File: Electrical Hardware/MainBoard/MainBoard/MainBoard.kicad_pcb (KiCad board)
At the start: 2 copper layers, 49.4 x 51.7 mm, 76 parts, among them J1 SM02B-SRSS-TB_LFSN_, J2 Conn_01x04_Socket, J3 Conn_01x04_Socket, J4 Conn_01x04_Socket, J5 USB_B_Micro, J6 Thermistor, J7 62684-401100ALF, J8 Conn_01x02_Socket, SW1 SW_Push, SW2 SW_Push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

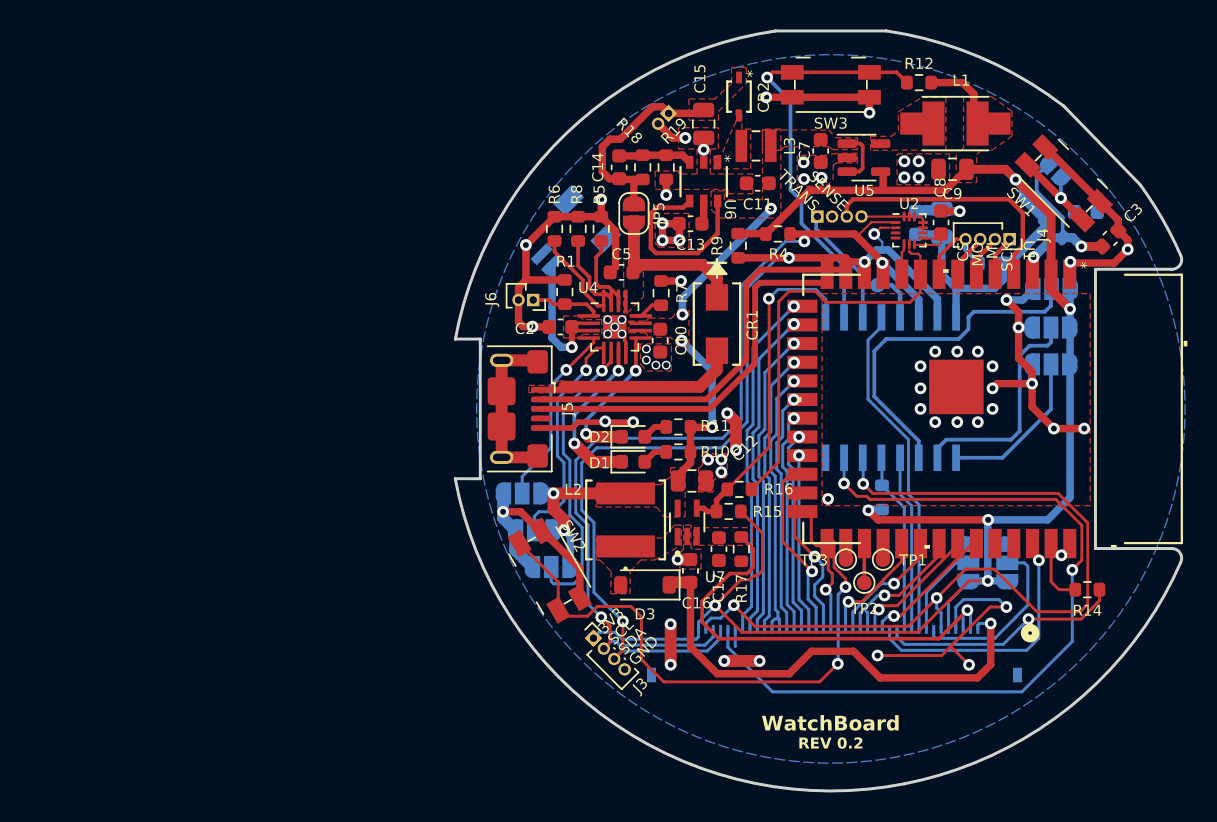
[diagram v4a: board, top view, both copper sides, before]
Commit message: Add potential new USB C port; make minor layout edits
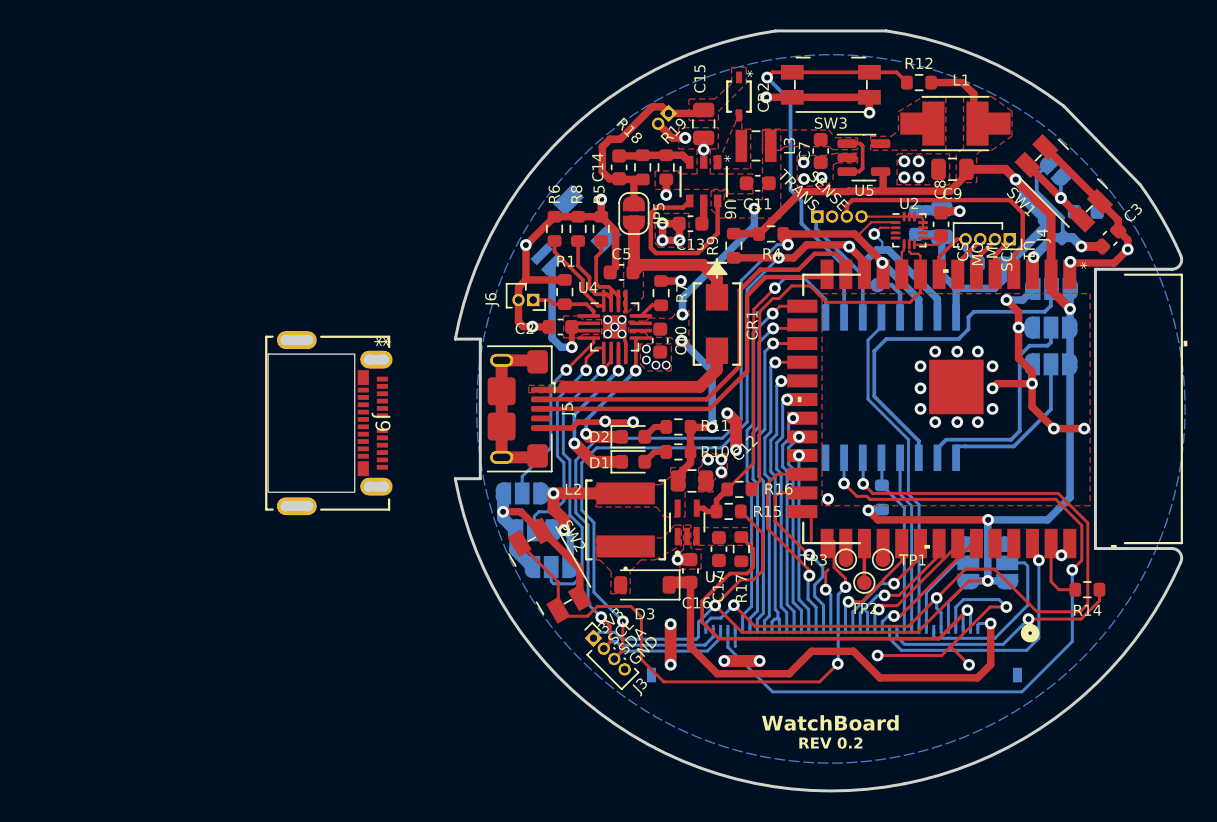
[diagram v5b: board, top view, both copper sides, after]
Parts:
- added J9: 1054550101, 1054550101:105455-0101_MOL, F.Cu at (59.5, 51.9)
- moved R4 0.46 mm to (89.7, 39.0)
- moved R9 0.30 mm to (87.1, 39.8)
- moved C8 0.13 mm to (101.2, 38.4)
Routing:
- net /B5: track 9.09 -> 6.26 mm
- net /G0: track 11.4 -> 13.5 mm
- net D-: track 28.2 -> 29.8 mm
- net /G1: track 13.4 -> 14.6 mm
- net /R3: track 21.9 -> 22.8 mm
- net /SDA: track 68.9 -> 69.7 mm
- net /BACKLIGHT: track 23.0 -> 23.7 mm
- net /R2: track 20.4 -> 21.2 mm
- net A1: track 27.6 -> 28.2 mm
- net /SCL: track 65.8 -> 66.5 mm
- net /R4: track 23.5 -> 24.1 mm
- net /R5: track 24.9 -> 25.4 mm
- net +3.3V: track 144.4 -> 144.9 mm
- net /R1: track 20.1 -> 20.6 mm

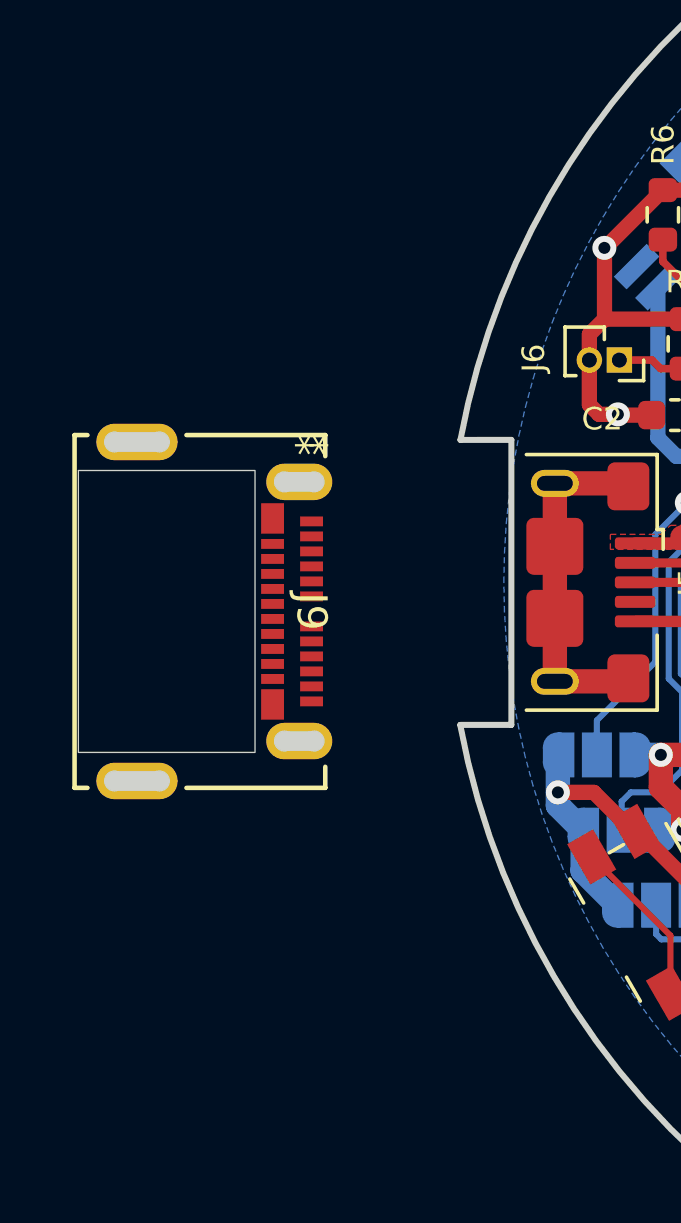
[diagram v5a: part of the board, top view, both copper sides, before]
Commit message: Add another potential USB-C with simplified pinout
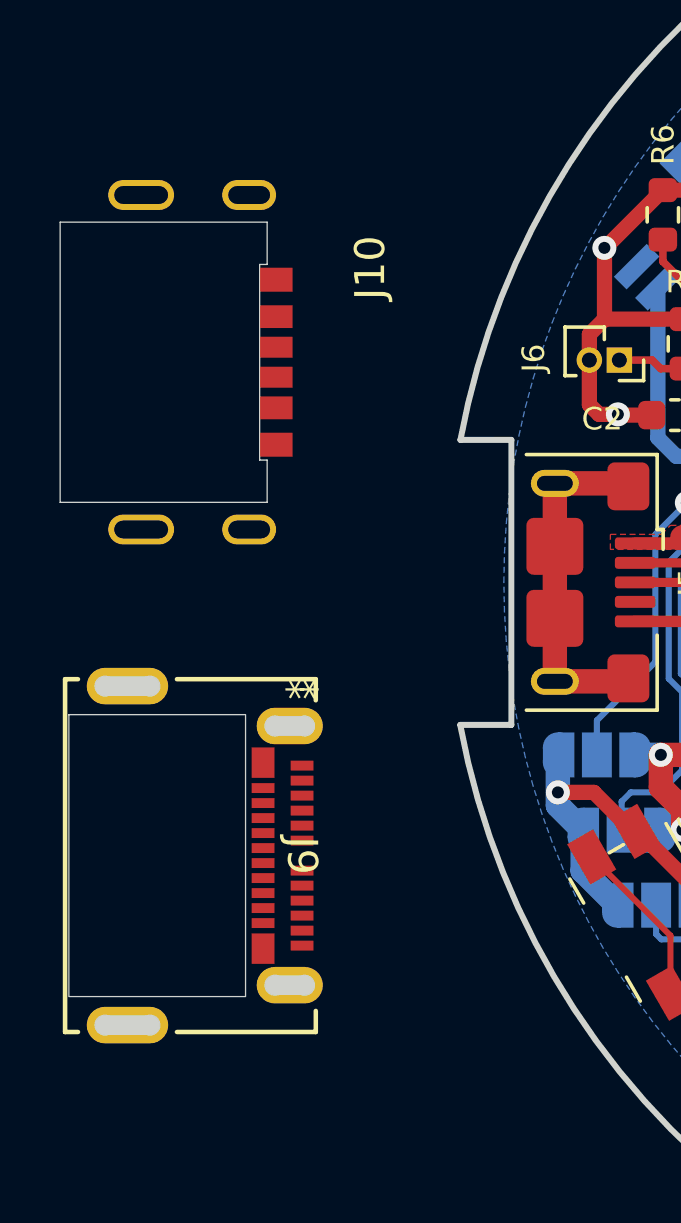
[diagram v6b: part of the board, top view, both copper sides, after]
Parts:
- added J10: UJC-HP-M-G-5-MSMT-TR, UJC_HP_M_G_5_MSMT_TR:CUI_UJC-HP-M-G-5-MSMT-TR, F.Cu at (57.5, 43.6)
- moved J9 8.14 mm to (59.2, 60.0)
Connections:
- J9 pad 25: unconnected-(J9-GND-Pad25) -> GND
- J9 pad 26: unconnected-(J9-GND-Pad26) -> GND
- J9 pad 27: unconnected-(J9-GND-Pad27) -> GND
- J9 pad 28: unconnected-(J9-GND-Pad28) -> GND
- J9 pad A1: unconnected-(J9-GND-PadA1) -> GND
- J9 pad A12: unconnected-(J9-GND-PadA12) -> GND
- J9 pad B1: unconnected-(J9-GND-PadB1) -> GND
- J9 pad B12: unconnected-(J9-GND-PadB12) -> GND

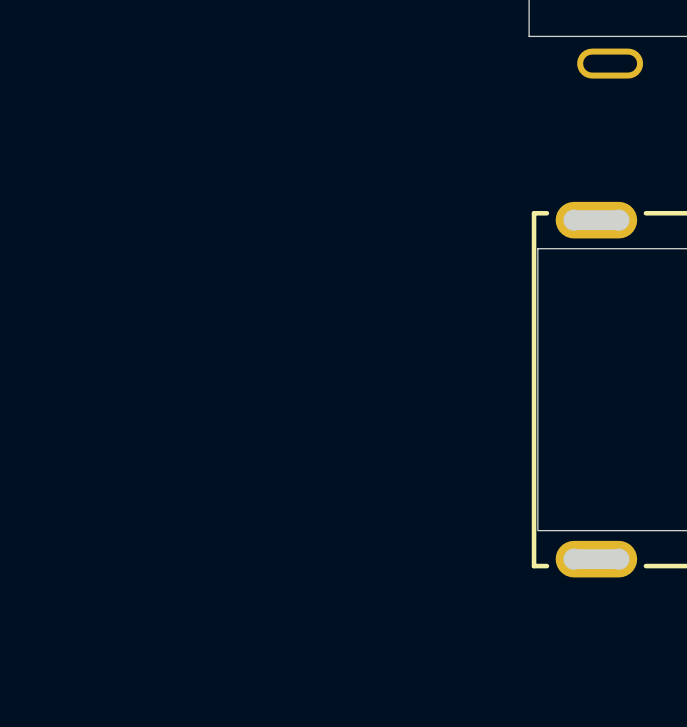
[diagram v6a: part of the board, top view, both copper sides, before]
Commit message: Add yet another USB-C, this time's the charm - simplified pinout but still for comms
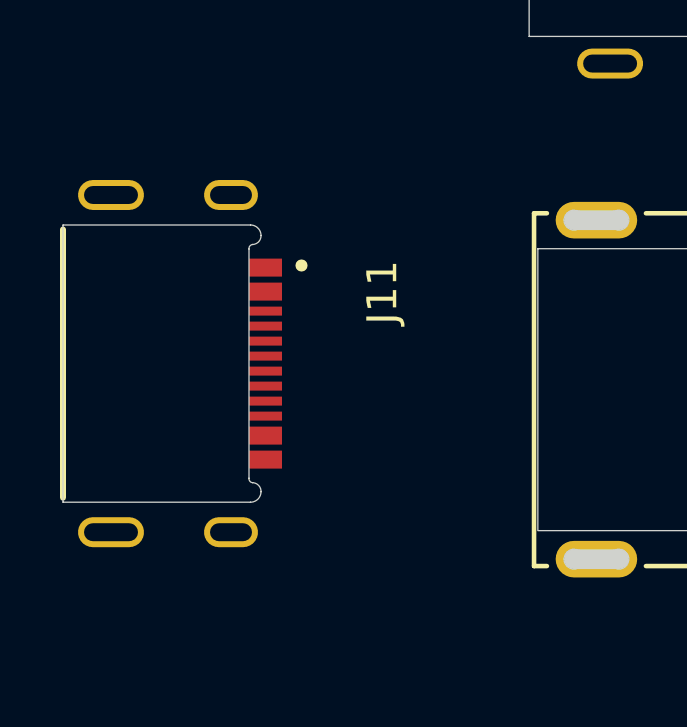
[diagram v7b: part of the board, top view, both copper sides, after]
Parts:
- added J11: USB4500-03-0-A_REVA1, USB4500-03-0-A:GCT_USB4500-03-0-A_REVA1, F.Cu at (40.9, 59.1)
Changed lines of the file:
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@@
   (net 109 "unconnected-(J10-SHIELD__2-PadSH3)")
   (net 110 "unconnected-(J10-SHIELD__3-PadSH4)")
+  (net 111 "unconnected-(J11-GND_A-PadA1_B12)")
+  (net 112 "unconnected-(J11-VBUS_A-PadA4_B9)")
+  (net 113 "unconnected-(J11-SBU2-PadB8)")
+  (net 114 "unconnected-(J11-CC1-PadA5)")
+  (net 115 "unconnected-(J11-DN2-PadB7)")
+  (net 116 "unconnected-(J11-DP1-PadA6)")
+  (net 117 "unconnected-(J11-DN1-PadA7)")
+  (net 118 "unconnected-(J11-DP2-PadB6)")
+  (net 119 "unconnected-(J11-SBU1-PadA8)")
+  (net 120 "unconnected-(J11-CC2-PadB5)")
+  (net 121 "unconnected-(J11-VBUS_B-PadB4_A9)")
+  (net 122 "unconnected-(J11-GND_B-PadB1_A12)")
+  (net 123 "unconnected-(J11-SHELL_GND-PadSH1)")
+  (net 124 "unconnected-(J11-SHELL_GND__1-PadSH2)")
+  (net 125 "unconnected-(J11-SHELL_GND__2-PadSH3)")
+  (net 126 "unconnected-(J11-SHELL_GND__3-PadSH4)")
   (footprint "Resistor_SMD:R_0603_1608Metric" (layer "F.Cu")
     (at 83.3467 52.1367)
@@
     )
   )
+  (footprint "USB4500-03-0-A:GCT_USB4500-03-0-A_REVA1" (layer "F.Cu")
+    (at 40.894 59.15 -90)
+    (property "MANUFACTURER" "Global Connector Technology")
+    (property "MAXIMUM_PACKAGE_HEIGHT" "2.36 mm")
+    (property "PARTREV" "A1")
+    (property "SNAPEDA_PN" "USB4500-03-0-A")
+    (property "STANDARD" "Manufacturer Recommendations")
+    (property "Sheetfile" "MainBoard.kicad_sch")
+    (property "Sheetname" "")
+    (attr smd)
+    (fp_text reference "J11" (at -2.375 -9.045 90) (layer "F.SilkS")
+        (effects (font (size 1 1) (thickness 0.15)))
+    )
+    (fp_text value "USB4500-03-0-A_REVA1" (at 9.79 -7.385 90) (layer "F.Fab")
+        (effects (font (size 1 1) (thickness 0.15)))
+    )
+    (fp_text user "PCB Edge" (at 6.46 1.49 90) (layer "F.Fab")
+        (effects (font (size 0.64 0.64) (thickness 0.15)))
+    )
+    (fp_line (start -4.47 1.6) (end 4.47 1.6)
+      (stroke (width 0.2) (type solid)) (layer "F.SilkS"))
+    (fp_circle (center -3.27 -6.35) (end -3.17 -6.35)
+      (stroke (width 0.2) (type solid)) (fill none) (layer "F.SilkS"))
+    (fp_line (start -4.62 -4.65) (end -4.62 1.6)
+      (stroke (width 0.01) (type solid)) (layer "Edge.Cuts"))
+    (fp_line (start -4.62 1.6) (end 4.62 1.6)
+      (stroke (width 0.01) (type solid)) (layer "Edge.Cuts"))
+    (fp_line (start 3.82 -4.6) (end -3.82 -4.6)
+      (stroke (width 0.01) (type solid)) (layer "Edge.Cuts"))
+    (fp_line (start 4.62 1.6) (end 4.62 -4.65)
+      (stroke (width 0.01) (type solid)) (layer "Edge.Cuts"))
+    (fp_arc (start -4.62 -4.65) (mid -4.517487 -4.897487) (end -4.27 -5)
+      (stroke (width 0.01) (type solid)) (layer "Edge.Cuts"))
+    (fp_arc (start -4.27 -5) (mid -4.06201 -4.922132) (end -3.97 -4.72)
+      (stroke (width 0.01) (type solid)) (layer "Edge.Cuts"))
+    (fp_arc (start -3.82 -4.6) (mid -3.919853 -4.628934) (end -3.97 -4.72)
+      (stroke (width 0.01) (type solid)) (layer "Edge.Cuts"))
+    (fp_arc (start 3.97 -4.72) (mid 3.919853 -4.628934) (end 3.82 -4.6)
+      (stroke (width 0.01) (type solid)) (layer "Edge.Cuts"))
+    (fp_arc (start 3.97 -4.72) (mid 4.06201 -4.922132) (end 4.27 -5)
+      (stroke (width 0.01) (type solid)) (layer "Edge.Cuts"))
+    (fp_arc (start 4.27 -5) (mid 4.517487 -4.897487) (end 4.62 -4.65)
+      (stroke (width 0.01) (type solid)) (layer "Edge.Cuts"))
+    (fp_line (start -6.37 -5.95) (end 6.37 -5.95)
+      (stroke (width 0.05) (type solid)) (layer "F.CrtYd"))
+    (fp_line (start -6.37 2.35) (end -6.37 -5.95)
+      (stroke (width 0.05) (type solid)) (layer "F.CrtYd"))
+    (fp_line (start -6.37 2.35) (end 6.37 2.35)
+      (stroke (width 0.05) (type solid)) (layer "F.CrtYd"))
+    (fp_line (start 6.37 2.35) (end 6.37 -5.95)
+      (stroke (width 0.05) (type solid)) (layer "F.CrtYd"))
+    (fp_line (start -6 1.6) (end 6 1.6)
+      (stroke (width 0.1) (type solid)) (layer "F.Fab"))
+    (fp_line (start -4.47 -4.4) (end 4.47 -4.4)
+      (stroke (width 0.1) (type solid)) (layer "F.Fab"))
+    (fp_line (start -4.47 2.1) (end -4.47 -4.4)
+      (stroke (width 0.1) (type solid)) (layer "F.Fab"))
+    (fp_line (start -4.47 2.1) (end 4.47 2.1)
+      (stroke (width 0.1) (type solid)) (layer "F.Fab"))
+    (fp_line (start 4.47 2.1) (end 4.47 -4.4)
+      (stroke (width 0.1) (type solid)) (layer "F.Fab"))
+    (fp_circle (center -3.27 -6.35) (end -3.17 -6.35)
+      (stroke (width 0.2) (type solid)) (fill none) (layer "F.Fab"))
+    (pad "A1_B12" smd rect (at -3.2 -5.15 270) (size 0.6 1.1) (layers "F.Cu" "F.Paste" "F.Mask")
+      (net 111 "unconnected-(J11-GND_A-PadA1_B12)") (pinfunction "GND_A") (pintype "power_in") (solder_mask_margin 0.102))
+    (pad "A4_B9" smd rect (at -2.4 -5.15 270) (size 0.6 1.1) (layers "F.Cu" "F.Paste" "F.Mask")
+      (net 112 "unconnected-(J11-VBUS_A-PadA4_B9)") (pinfunction "VBUS_A") (pintype "power_in") (solder_mask_margin 0.102))
+    (pad "A5" smd rect (at -1.25 -5.15 270) (size 0.3 1.1) (layers "F.Cu" "F.Paste" "F.Mask")
+      (net 114 "unconnected-(J11-CC1-PadA5)") (pinfunction "CC1") (pintype "bidirectional") (solder_mask_margin 0.102))
+    (pad "A6" smd rect (at -0.25 -5.15 270) (size 0.3 1.1) (layers "F.Cu" "F.Paste" "F.Mask")
+      (net 116 "unconnected-(J11-DP1-PadA6)") (pinfunction "DP1") (pintype "bidirectional") (solder_mask_margin 0.102))
+    (pad "A7" smd rect (at 0.25 -5.15 270) (size 0.3 1.1) (layers "F.Cu" "F.Paste" "F.Mask")
+      (net 117 "unconnected-(J11-DN1-PadA7)") (pinfunction "DN1") (pintype "bidirectional") (solder_mask_margin 0.102))
+    (pad "A8" smd rect (at 1.25 -5.15 270) (size 0.3 1.1) (layers "F.Cu" "F.Paste" "F.Mask")
+      (net 119 "unconnected-(J11-SBU1-PadA8)") (pinfunction "SBU1") (pintype "bidirectional") (solder_mask_margin 0.102))
+    (pad "B1_A12" smd rect (at 3.2 -5.15 270) (size 0.6 1.1) (layers "F.Cu" "F.Paste" "F.Mask")
+      (net 122 "unconnected-(J11-GND_B-PadB1_A12)") (pinfunction "GND_B") (pintype "power_in") (solder_mask_margin 0.102))
+    (pad "B4_A9" smd rect (at 2.4 -5.15 270) (size 0.6 1.1) (layers "F.Cu" "F.Paste" "F.Mask")
+      (net 121 "unconnected-(J11-VBUS_B-PadB4_A9)") (pinfunction "VBUS_B") (pintype "power_in") (solder_mask_margin 0.102))
+    (pad "B5" smd rect (at 1.75 -5.15 270) (size 0.3 1.1) (layers "F.Cu" "F.Paste" "F.Mask")
+      (net 120 "unconnected-(J11-CC2-PadB5)") (pinfunction "CC2") (pintype "bidirectional") (solder_mask_margin 0.102))
+    (pad "B6" smd rect (at 0.75 -5.15 270) (size 0.3 1.1) (layers "F.Cu" "F.Paste" "F.Mask")
+      (net 118 "unconnected-(J11-DP2-PadB6)") (pinfunction "DP2") (pintype "bidirectional") (solder_mask_margin 0.102))
+    (pad "B7" smd rect (at -0.75 -5.15 270) (size 0.3 1.1) (layers "F.Cu" "F.Paste" "F.Mask")
+      (net 115 "unconnected-(J11-DN2-PadB7)") (pinfunction "DN2") (pintype "bidirectional") (solder_mask_margin 0.102))
+    (pad "B8" smd rect (at -1.75 -5.15 270) (size 0.3 1.1) (layers "F.Cu" "F.Paste" "F.Mask")
+      (net 113 "unconnected-(J11-SBU2-PadB8)") (pinfunction "SBU2") (pintype "bidirectional") (solder_mask_margin 0.102))
+    (pad "SH1" thru_hole oval (at -5.62 0 270) (size 1 2.2) (drill oval 0.6 1.8) (layers "*.Cu" "*.Mask")
+      (net 123 "unconnected-(J11-SHELL_GND-PadSH1)") (pinfunction "SHELL_GND") (pintype "power_in") (solder_mask_margin 0.102))
+    (pad "SH2" thru_hole oval (at 5.62 -4 270) (size 1 1.8) (drill oval 0.6 1.4) (layers "*.Cu" "*.Mask")
+      (net 124 "unconnected-(J11-SHELL_GND__1-PadSH2)") (pinfunction "SHELL_GND__1") (pintype "power_in") (solder_mask_margin 0.102))
+    (pad "SH3" thru_hole oval (at -5.62 -4 270) (size 1 1.8) (drill oval 0.6 1.4) (layers "*.Cu" "*.Mask")
+      (net 125 "unconnected-(J11-SHELL_GND__2-PadSH3)") (pinfunction "SHELL_GND__2") (pintype "power_in") (solder_mask_margin 0.102))
+    (pad "SH4" thru_hole oval (at 5.62 0 270) (size 1 2.2) (drill oval 0.6 1.8) (layers "*.Cu" "*.Mask")
+      (net 126 "unconnected-(J11-SHELL_GND__3-PadSH4)") (pinfunction "SHELL_GND__3") (pintype "power_in") (solder_mask_margin 0.102))
+  )
   (footprint "NR5040T6R8M:IND_TAIYO_NR5040_TAY" (layer "F.Cu")
